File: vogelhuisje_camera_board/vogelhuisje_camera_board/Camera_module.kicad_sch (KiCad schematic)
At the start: 18 parts, among them J4 Camera Connector, Q2 Q_NMOS_DSG, U1 XC6206-2.8V, U2 XC6206-1.2V

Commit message: Kicad Changes Tadjiro
Board now supports 3 lipo cells and a motion sensor.
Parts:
- added JMotion1: Conn_01x03_Female, Connector_PinHeader_2.54mm:PinHeader_1x03_P2.54mm_Vertical, symbol Connector:Conn_01x03_Female
- 100n1: renamed from C1; value 100n -> 100nF; footprint Capacitor_SMD:C_0201_0603Metric_Pad0.64x0.40mm_HandSolder -> Capacitor_THT:C_Axial_L5.1mm_D3.1mm_P7.50mm_Horizontal
- 15pf1: renamed from C2; footprint Capacitor_SMD:C_01005_0402Metric_Pad0.57x0.30mm_HandSolder -> Capacitor_THT:C_Axial_L5.1mm_D3.1mm_P7.50mm_Horizontal
- C100n2: renamed from C4; footprint Capacitor_SMD:C_0603_1608Metric_Pad1.08x0.95mm_HandSolder -> Capacitor_THT:C_Axial_L5.1mm_D3.1mm_P7.50mm_Horizontal
- C100n3: renamed from C6; footprint Capacitor_SMD:C_0603_1608Metric_Pad1.08x0.95mm_HandSolder -> Capacitor_THT:C_Axial_L5.1mm_D3.1mm_P7.50mm_Horizontal
- C10u1: renamed from C5; footprint Capacitor_SMD:C_0805_2012Metric_Pad1.18x1.45mm_HandSolder -> Capacitor_THT:C_Axial_L5.1mm_D3.1mm_P7.50mm_Horizontal
- C10u2: renamed from C7; footprint Capacitor_SMD:C_0805_2012Metric_Pad1.18x1.45mm_HandSolder -> Capacitor_THT:C_Axial_L5.1mm_D3.1mm_P7.50mm_Horizontal
- C10u3: renamed from C3; footprint Capacitor_SMD:C_0805_2012Metric_Pad1.18x1.45mm_HandSolder -> Capacitor_THT:C_Axial_L5.1mm_D3.1mm_P7.50mm_Horizontal
- R1k1: renamed from R1; value 1k -> 1k1
- URegulator1.2: renamed from U2; value XC6206-1.2V -> 1.2V Regulator; footprint Package_TO_SOT_SMD:SOT-23 -> Package_TO_SOT_THT:TO-92
- URegulator2.8: renamed from U1; value XC6206-2.8V -> 2.8V regulator; footprint Package_TO_SOT_SMD:SOT-23 -> Package_TO_SOT_THT:TO-92
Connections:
- net 3V3: now also JMotion1.1 (Pin_1)
- net GND: now also JMotion1.3 (Pin_3)
- new net Motion_out: JMotion1.2 (Pin_2)
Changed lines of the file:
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@@
     (effects (font (size 1.27 1.27)) (justify left))
+  )
+  (hierarchical_label "Motion_out" (shape input) (at 175.26 125.73 180)
+    (effects (font (size 1.27 1.27)) (justify right))
   )
   (hierarchical_label "V_led_switch-" (shape input) (at 240.03 104.14 0)
@@
   (hierarchical_label "TWI_SCK" (shape input) (at 100.33 76.2 0)
     (effects (font (size 1.27 1.27)) (justify left))
+  )
+  (hierarchical_label "3V3" (shape input) (at 175.26 123.19 180)
+    (effects (font (size 1.27 1.27)) (justify right))
   )
   (hierarchical_label "CSI_HSYNC" (shape input) (at 100.33 86.36 0)
@@
   (symbol (lib_id "Device:C") (at 116.84 106.68 270) (unit 1)
     (in_bom yes) (on_board yes)
-    (property "Reference" "C2" (id 0) (at 116.84 100.2792 90))
+    (property "Reference" "15pf1" (id 0) (at 116.84 100.2792 90))
     (property "Value" "15pF" (id 1) (at 116.84 102.5906 90))
-    (property "Footprint" "Capacitor_SMD:C_01005_0402Metric_Pad0.57x0.30mm_HandSolder" (id 2) (at 113.03 107.6452 0)
+    (property "Footprint" "Capacitor_THT:C_Axial_L5.1mm_D3.1mm_P7.50mm_Horizontal" (id 2) (at 113.03 107.6452 0)
       (effects (font (size 1.27 1.27)) hide)
     )
@@
   (symbol (lib_id "Device:C") (at 116.84 91.44 270) (unit 1)
     (in_bom yes) (on_board yes)
-    (property "Reference" "C1" (id 0) (at 116.84 85.0392 90))
-    (property "Value" "100n" (id 1) (at 116.84 87.3506 90))
-    (property "Footprint" "Capacitor_SMD:C_0201_0603Metric_Pad0.64x0.40mm_HandSolder" (id 2) (at 113.03 92.4052 0)
+    (property "Reference" "100n1" (id 0) (at 116.84 85.0392 90))
+    (property "Value" "100nF" (id 1) (at 116.84 87.3506 90))
+    (property "Footprint" "Capacitor_THT:C_Axial_L5.1mm_D3.1mm_P7.50mm_Horizontal" (id 2) (at 113.03 92.4052 0)
       (effects (font (size 1.27 1.27)) hide)
     )
@@
   (symbol (lib_id "Device:R") (at 118.11 83.82 270) (unit 1)
     (in_bom yes) (on_board yes)
-    (property "Reference" "R1" (id 0) (at 118.11 78.5622 90))
-    (property "Value" "1k" (id 1) (at 118.11 80.8736 90))
+    (property "Reference" "R1k1" (id 0) (at 118.11 78.5622 90))
+    (property "Value" "1k1" (id 1) (at 118.11 80.8736 90))
     (property "Footprint" "Resistor_THT:R_Axial_DIN0207_L6.3mm_D2.5mm_P10.16mm_Horizontal" (id 2) (at 118.11 82.042 90)
       (effects (font (size 1.27 1.27)) hide)
@@
   (symbol (lib_id "Regulator_Linear:XC6206PxxxMR") (at 168.91 74.93 0) (unit 1)
     (in_bom yes) (on_board yes)
-    (property "Reference" "U1" (id 0) (at 168.91 68.7832 0))
-    (property "Value" "XC6206-2.8V" (id 1) (at 168.91 71.0946 0))
-    (property "Footprint" "Package_TO_SOT_SMD:SOT-23" (id 2) (at 168.91 69.215 0)
+    (property "Reference" "URegulator2.8" (id 0) (at 168.91 68.7832 0))
+    (property "Value" "2.8V regulator" (id 1) (at 168.91 71.0946 0))
+    (property "Footprint" "Package_TO_SOT_THT:TO-92" (id 2) (at 168.91 69.215 0)
       (effects (font (size 1.27 1.27) italic) hide)
     )
@@
   (symbol (lib_id "Regulator_Linear:XC6206PxxxMR") (at 168.91 96.52 0) (unit 1)
     (in_bom yes) (on_board yes)
-    (property "Reference" "U2" (id 0) (at 168.91 90.3732 0))
-    (property "Value" "XC6206-1.2V" (id 1) (at 168.91 92.6846 0))
-    (property "Footprint" "Package_TO_SOT_SMD:SOT-23" (id 2) (at 168.91 90.805 0)
+    (property "Reference" "URegulator1.2" (id 0) (at 168.91 90.3732 0))
+    (property "Value" "1.2V Regulator" (id 1) (at 168.91 92.6846 0))
+    (property "Footprint" "Package_TO_SOT_THT:TO-92" (id 2) (at 168.91 90.805 0)
       (effects (font (size 1.27 1.27) italic) hide)
     )
@@
   (symbol (lib_id "Device:C") (at 158.75 100.33 0) (unit 1)
     (in_bom yes) (on_board yes)
-    (property "Reference" "C7" (id 0) (at 161.671 99.1616 0)
+    (property "Reference" "C10u2" (id 0) (at 161.671 99.1616 0)
       (effects (font (size 1.27 1.27)) (justify left))
     )
@@
       (effects (font (size 1.27 1.27)) (justify left))
     )
-    (property "Footprint" "Capacitor_SMD:C_0805_2012Metric_Pad1.18x1.45mm_HandSolder" (id 2) (at 159.7152 104.14 0)
+    (property "Footprint" "Capacitor_THT:C_Axial_L5.1mm_D3.1mm_P7.50mm_Horizontal" (id 2) (at 159.7152 104.14 0)
       (effects (font (size 1.27 1.27)) hide)
     )
@@
   (symbol (lib_id "Device:C") (at 182.88 78.74 0) (unit 1)
     (in_bom yes) (on_board yes)
-    (property "Reference" "C3" (id 0) (at 185.801 77.5716 0)
+    (property "Reference" "C10u3" (id 0) (at 185.801 77.5716 0)
       (effects (font (size 1.27 1.27)) (justify left))
     )
@@
       (effects (font (size 1.27 1.27)) (justify left))
     )
-    (property "Footprint" "Capacitor_SMD:C_0805_2012Metric_Pad1.18x1.45mm_HandSolder" (id 2) (at 183.8452 82.55 0)
+    (property "Footprint" "Capacitor_THT:C_Axial_L5.1mm_D3.1mm_P7.50mm_Horizontal" (id 2) (at 183.8452 82.55 0)
       (effects (font (size 1.27 1.27)) hide)
     )
@@
   (symbol (lib_id "Device:C") (at 190.5 78.74 0) (unit 1)
     (in_bom yes) (on_board yes)
-    (property "Reference" "C4" (id 0) (at 193.421 77.5716 0)
+    (property "Reference" "C100n2" (id 0) (at 193.421 77.5716 0)
       (effects (font (size 1.27 1.27)) (justify left))
     )
@@
       (effects (font (size 1.27 1.27)) (justify left))
     )
-    (property "Footprint" "Capacitor_SMD:C_0603_1608Metric_Pad1.08x0.95mm_HandSolder" (id 2) (at 191.4652 82.55 0)
+    (property "Footprint" "Capacitor_THT:C_Axial_L5.1mm_D3.1mm_P7.50mm_Horizontal" (id 2) (at 191.4652 82.55 0)
       (effects (font (size 1.27 1.27)) hide)
     )
@@
   (symbol (lib_id "Device:C") (at 181.61 100.33 0) (unit 1)
     (in_bom yes) (on_board yes)
-    (property "Reference" "C5" (id 0) (at 184.531 99.1616 0)
+    (property "Reference" "C10u1" (id 0) (at 184.531 99.1616 0)
       (effects (font (size 1.27 1.27)) (justify left))
     )
@@
       (effects (font (size 1.27 1.27)) (justify left))
     )
-    (property "Footprint" "Capacitor_SMD:C_0805_2012Metric_Pad1.18x1.45mm_HandSolder" (id 2) (at 182.5752 104.14 0)
+    (property "Footprint" "Capacitor_THT:C_Axial_L5.1mm_D3.1mm_P7.50mm_Horizontal" (id 2) (at 182.5752 104.14 0)
       (effects (font (size 1.27 1.27)) hide)
     )
@@
   (symbol (lib_id "Device:C") (at 189.23 100.33 0) (unit 1)
     (in_bom yes) (on_board yes)
-    (property "Reference" "C6" (id 0) (at 192.151 99.1616 0)
+    (property "Reference" "C100n3" (id 0) (at 192.151 99.1616 0)
       (effects (font (size 1.27 1.27)) (justify left))
     )
@@
       (effects (font (size 1.27 1.27)) (justify left))
     )
-    (property "Footprint" "Capacitor_SMD:C_0603_1608Metric_Pad1.08x0.95mm_HandSolder" (id 2) (at 190.1952 104.14 0)
+    (property "Footprint" "Capacitor_THT:C_Axial_L5.1mm_D3.1mm_P7.50mm_Horizontal" (id 2) (at 190.1952 104.14 0)
       (effects (font (size 1.27 1.27)) hide)
     )
@@
     (pin "2")
   )
+  (symbol (lib_id "Connector:Conn_01x03_Female") (at 180.34 125.73 0) (unit 1)
+    (in_bom yes) (on_board yes) (fields_autoplaced)
+    (property "Reference" "JMotion1" (id 0) (at 181.0512 124.8953 0)
+      (effects (font (size 1.27 1.27)) (justify left))
+    )
+    (property "Value" "Conn_01x03_Female" (id 1) (at 181.0512 127.4322 0)
+      (effects (font (size 1.27 1.27)) (justify left))
+    )
+    (property "Footprint" "Connector_PinHeader_2.54mm:PinHeader_1x03_P2.54mm_Vertical" (id 2) (at 180.34 125.73 0)
+      (effects (font (size 1.27 1.27)) hide)
+    )
+    (property "Datasheet" "~" (id 3) (at 180.34 125.73 0)
+      (effects (font (size 1.27 1.27)) hide)
+    )
+    (pin "1")
+    (pin "2")
+    (pin "3")
+  )
+  (symbol (lib_id "power:GND") (at 175.26 128.27 0) (unit 1)
+    (in_bom yes) (on_board yes) (fields_autoplaced)
+    (property "Reference" "#PWR0101" (id 0) (at 175.26 134.62 0)
+      (effects (font (size 1.27 1.27)) hide)
+    )
+    (property "Value" "GND" (id 1) (at 175.26 132.7134 0))
+    (property "Footprint" "" (id 2) (at 175.26 128.27 0)
+      (effects (font (size 1.27 1.27)) hide)
+    )
+    (property "Datasheet" "" (id 3) (at 175.26 128.27 0)
+      (effects (font (size 1.27 1.27)) hide)
+    )
+    (pin "1")
+  )
 )

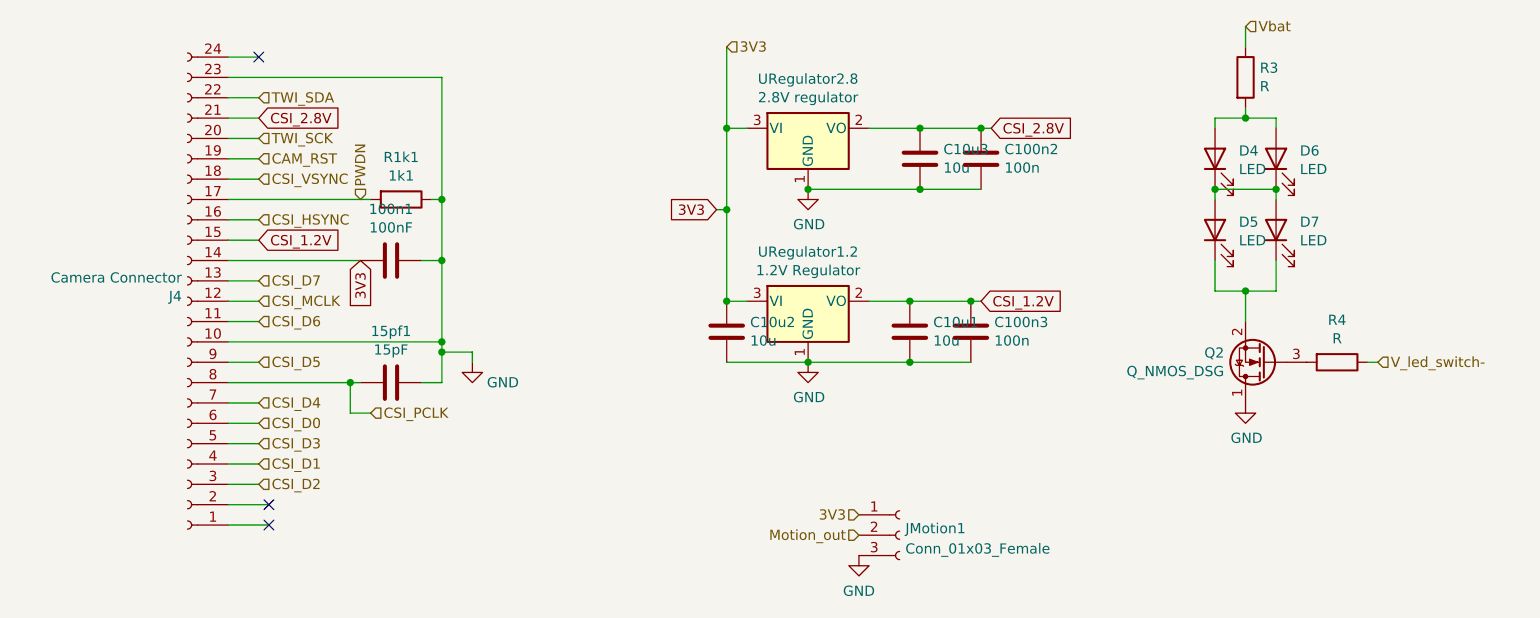
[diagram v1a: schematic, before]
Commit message: Updated Camera Board
Moved capacitors close to LDO output, corrected capacitor values and ported ground from the main board.
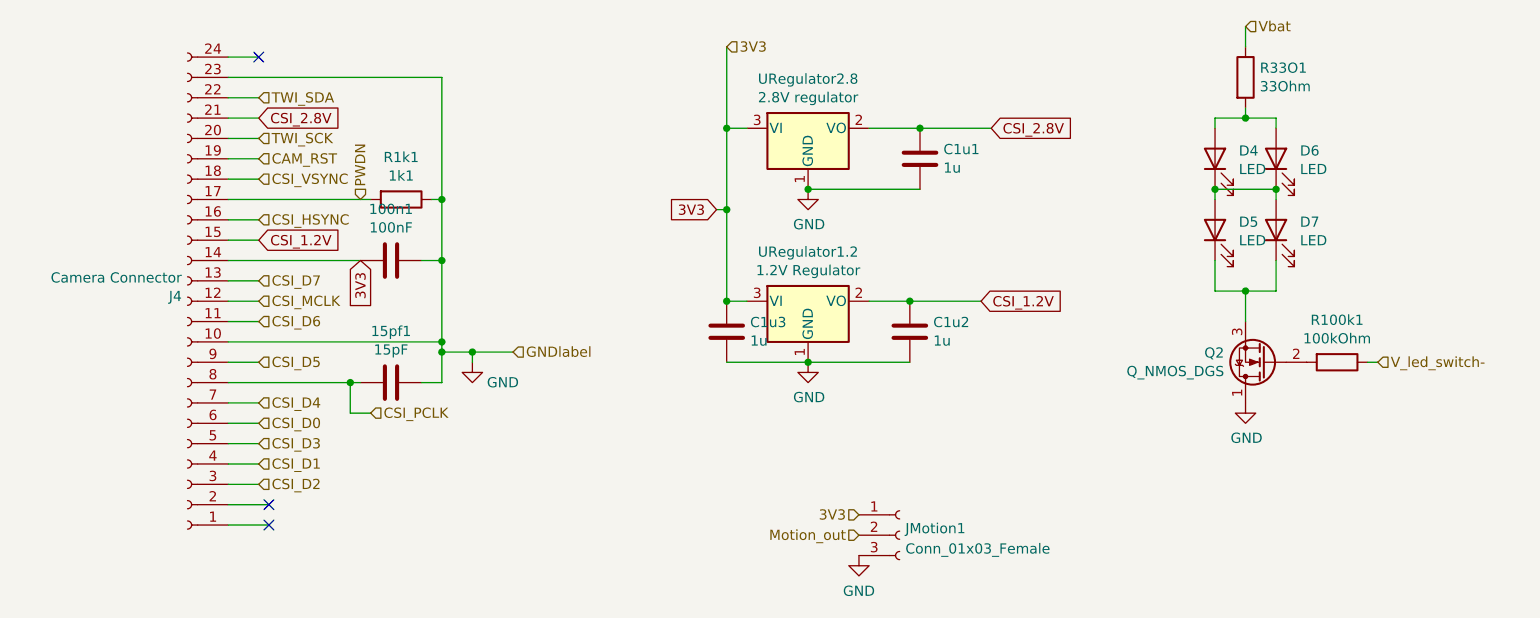
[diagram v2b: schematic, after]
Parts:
- removed C100n2, C100n3: 100n, Capacitor_THT:C_Axial_L5.1mm_D3.1mm_P7.50mm_Horizontal, symbol Device:C
- C1u1: renamed from C10u3; value 10u -> 1u
- C1u2: renamed from C10u1; value 10u -> 1u
- C1u3: renamed from C10u2; value 10u -> 1u
- Q2: value Q_NMOS_DSG -> Q_NMOS_DGS; symbol Device:Q_NMOS_DSG -> Device:Q_NMOS_DGS
- R100k1: renamed from R4; value R -> 100kOhm
- R33O1: renamed from R3; value R -> 33Ohm
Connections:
- net at R100k1.2: now also Q2.2 (G); no longer Q2.3 (G)
- net at D5.1 (K), D7.1 (K): now also Q2.3 (S); no longer Q2.2 (S)
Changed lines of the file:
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@@
   (junction (at 223.52 73.66) (diameter 0) (color 0 0 0 0)
   )
+  (junction (at 127 102.87) (diameter 0) (color 0 0 0 0)
+  )
   (junction (at 158.75 74.93) (diameter 0) (color 0 0 0 0)
   )
@@
   (junction (at 182.88 74.93) (diameter 0) (color 0 0 0 0)
   )
-  (junction (at 189.23 96.52) (diameter 0) (color 0 0 0 0)
-  )
   (junction (at 158.75 96.52) (diameter 0) (color 0 0 0 0)
   )
@@
   (junction (at 123.19 101.6) (diameter 0) (color 0 0 0 0)
   )
-  (junction (at 182.88 82.55) (diameter 0) (color 0 0 0 0)
-  )
-  (junction (at 181.61 104.14) (diameter 0) (color 0 0 0 0)
-  )
   (junction (at 223.52 95.25) (diameter 0) (color 0 0 0 0)
   )
@@
   )
   (junction (at 219.71 82.55) (diameter 0) (color 0 0 0 0)
-  )
-  (junction (at 190.5 74.93) (diameter 0) (color 0 0 0 0)
   )
   (no_connect (at 101.6 124.46))
   (no_connect (at 101.6 121.92))
   (no_connect (at 100.33 66.04))
-  (wire (pts (xy 190.5 96.52) (xy 189.23 96.52))
-    (stroke (width 0) (type default) (color 0 0 0 0))
-  )
   (wire (pts (xy 158.75 104.14) (xy 168.91 104.14))
     (stroke (width 0) (type default) (color 0 0 0 0))
@@
     (stroke (width 0) (type default) (color 0 0 0 0))
   )
-  (wire (pts (xy 182.88 82.55) (xy 190.5 82.55))
-    (stroke (width 0) (type default) (color 0 0 0 0))
-  )
   (wire (pts (xy 157.48 85.09) (xy 158.75 85.09))
     (stroke (width 0) (type default) (color 0 0 0 0))
@@
     (stroke (width 0) (type default) (color 0 0 0 0))
   )
-  (wire (pts (xy 191.77 74.93) (xy 190.5 74.93))
+  (wire (pts (xy 182.88 74.93) (xy 191.77 74.93))
     (stroke (width 0) (type default) (color 0 0 0 0))
   )
@@
     (stroke (width 0) (type default) (color 0 0 0 0))
   )
+  (wire (pts (xy 127 102.87) (xy 132.08 102.87))
+    (stroke (width 0) (type default) (color 0 0 0 0))
+  )
   (wire (pts (xy 223.52 72.39) (xy 223.52 73.66))
     (stroke (width 0) (type default) (color 0 0 0 0))
   )
-  (wire (pts (xy 189.23 104.14) (xy 181.61 104.14))
-    (stroke (width 0) (type default) (color 0 0 0 0))
-  )
   (wire (pts (xy 100.33 66.04) (xy 96.52 66.04))
     (stroke (width 0) (type default) (color 0 0 0 0))
@@
     (stroke (width 0) (type default) (color 0 0 0 0))
   )
-  (wire (pts (xy 181.61 96.52) (xy 189.23 96.52))
+  (wire (pts (xy 181.61 96.52) (xy 190.5 96.52))
     (stroke (width 0) (type default) (color 0 0 0 0))
   )
@@
   )
   (wire (pts (xy 181.61 104.14) (xy 168.91 104.14))
-    (stroke (width 0) (type default) (color 0 0 0 0))
-  )
-  (wire (pts (xy 190.5 74.93) (xy 182.88 74.93))
     (stroke (width 0) (type default) (color 0 0 0 0))
   )
@@
     (effects (font (size 1.27 1.27)) (justify left))
   )
+  (hierarchical_label "GNDlabel" (shape input) (at 132.08 102.87 0)
+    (effects (font (size 1.27 1.27)) (justify left))
+  )
   (hierarchical_label "3V3" (shape input) (at 175.26 123.19 180)
     (effects (font (size 1.27 1.27)) (justify right))
@@
   (symbol (lib_id "Device:R") (at 234.95 104.14 270) (unit 1)
     (in_bom yes) (on_board yes)
-    (property "Reference" "R4" (id 0) (at 234.95 98.8822 90))
-    (property "Value" "R" (id 1) (at 234.95 101.1936 90))
+    (property "Reference" "R100k1" (id 0) (at 234.95 98.8822 90))
+    (property "Value" "100kOhm" (id 1) (at 234.95 101.1936 90))
     (property "Footprint" "Resistor_THT:R_Axial_DIN0207_L6.3mm_D2.5mm_P10.16mm_Horizontal" (id 2) (at 234.95 102.362 90)
       (effects (font (size 1.27 1.27)) hide)
@@
     (pin "2")
   )
-  (symbol (lib_id "Device:Q_NMOS_DSG") (at 226.06 104.14 180) (unit 1)
+  (symbol (lib_id "Device:Q_NMOS_DGS") (at 226.06 104.14 180) (unit 1)
     (in_bom yes) (on_board yes)
     (property "Reference" "Q2" (id 0) (at 220.853 102.9716 0)
       (effects (font (size 1.27 1.27)) (justify left))
     )
-    (property "Value" "Q_NMOS_DSG" (id 1) (at 220.853 105.283 0)
+    (property "Value" "Q_NMOS_DGS" (id 1) (at 220.853 105.283 0)
       (effects (font (size 1.27 1.27)) (justify left))
     )
@@
   (symbol (lib_id "Device:R") (at 223.52 68.58 0) (unit 1)
     (in_bom yes) (on_board yes)
-    (property "Reference" "R3" (id 0) (at 225.298 67.4116 0)
-      (effects (font (size 1.27 1.27)) (justify left))
-    )
-    (property "Value" "R" (id 1) (at 225.298 69.723 0)
+    (property "Reference" "R33O1" (id 0) (at 225.298 67.4116 0)
+      (effects (font (size 1.27 1.27)) (justify left))
+    )
+    (property "Value" "33Ohm" (id 1) (at 225.298 69.723 0)
       (effects (font (size 1.27 1.27)) (justify left))
     )
@@
   (symbol (lib_id "Device:C") (at 158.75 100.33 0) (unit 1)
     (in_bom yes) (on_board yes)
-    (property "Reference" "C10u2" (id 0) (at 161.671 99.1616 0)
-      (effects (font (size 1.27 1.27)) (justify left))
-    )
-    (property "Value" "10u" (id 1) (at 161.671 101.473 0)
+    (property "Reference" "C1u3" (id 0) (at 161.671 99.1616 0)
+      (effects (font (size 1.27 1.27)) (justify left))
+    )
+    (property "Value" "1u" (id 1) (at 161.671 101.473 0)
       (effects (font (size 1.27 1.27)) (justify left))
     )
@@
   (symbol (lib_id "Device:C") (at 182.88 78.74 0) (unit 1)
     (in_bom yes) (on_board yes)
-    (property "Reference" "C10u3" (id 0) (at 185.801 77.5716 0)
-      (effects (font (size 1.27 1.27)) (justify left))
-    )
-    (property "Value" "10u" (id 1) (at 185.801 79.883 0)
+    (property "Reference" "C1u1" (id 0) (at 185.801 77.5716 0)
+      (effects (font (size 1.27 1.27)) (justify left))
+    )
+    (property "Value" "1u" (id 1) (at 185.801 79.883 0)
       (effects (font (size 1.27 1.27)) (justify left))
     )
@@
     (pin "2")
   )
-  (symbol (lib_id "Device:C") (at 190.5 78.74 0) (unit 1)
-    (in_bom yes) (on_board yes)
-    (property "Reference" "C100n2" (id 0) (at 193.421 77.5716 0)
-      (effects (font (size 1.27 1.27)) (justify left))
-    )
-    (property "Value" "100n" (id 1) (at 193.421 79.883 0)
-      (effects (font (size 1.27 1.27)) (justify left))
-    )
-    (property "Footprint" "Capacitor_THT:C_Axial_L5.1mm_D3.1mm_P7.50mm_Horizontal" (id 2) (at 191.4652 82.55 0)
-      (effects (font (size 1.27 1.27)) hide)
-    )
-    (property "Datasheet" "~" (id 3) (at 190.5 78.74 0)
-      (effects (font (size 1.27 1.27)) hide)
-    )
-    (pin "1")
-    (pin "2")
-  )
   (symbol (lib_id "Device:C") (at 181.61 100.33 0) (unit 1)
     (in_bom yes) (on_board yes)
-    (property "Reference" "C10u1" (id 0) (at 184.531 99.1616 0)
-      (effects (font (size 1.27 1.27)) (justify left))
-    )
-    (property "Value" "10u" (id 1) (at 184.531 101.473 0)
+    (property "Reference" "C1u2" (id 0) (at 184.531 99.1616 0)
+      (effects (font (size 1.27 1.27)) (justify left))
+    )
+    (property "Value" "1u" (id 1) (at 184.531 101.473 0)
       (effects (font (size 1.27 1.27)) (justify left))
     )
@@
       (effects (font (size 1.27 1.27)) hide)
     )
-    (pin "1")
-    (pin "2")
-  )
-  (symbol (lib_id "Device:C") (at 189.23 100.33 0) (unit 1)
-    (in_bom yes) (on_board yes)
-    (property "Reference" "C100n3" (id 0) (at 192.151 99.1616 0)
-      (effects (font (size 1.27 1.27)) (justify left))
-    )
-    (property "Value" "100n" (id 1) (at 192.151 101.473 0)
-      (effects (font (size 1.27 1.27)) (justify left))
-    )
-    (property "Footprint" "Capacitor_THT:C_Axial_L5.1mm_D3.1mm_P7.50mm_Horizontal" (id 2) (at 190.1952 104.14 0)
-      (effects (font (size 1.27 1.27)) hide)
-    )
-    (property "Datasheet" "~" (id 3) (at 189.23 100.33 0)
-      (effects (font (size 1.27 1.27)) hide)
-    )
